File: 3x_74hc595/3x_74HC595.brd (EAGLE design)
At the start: 61 x 19.1 mm, 12 parts, among them IC1 74HC595D, IC2 74HC595D, IC3 74HC595D

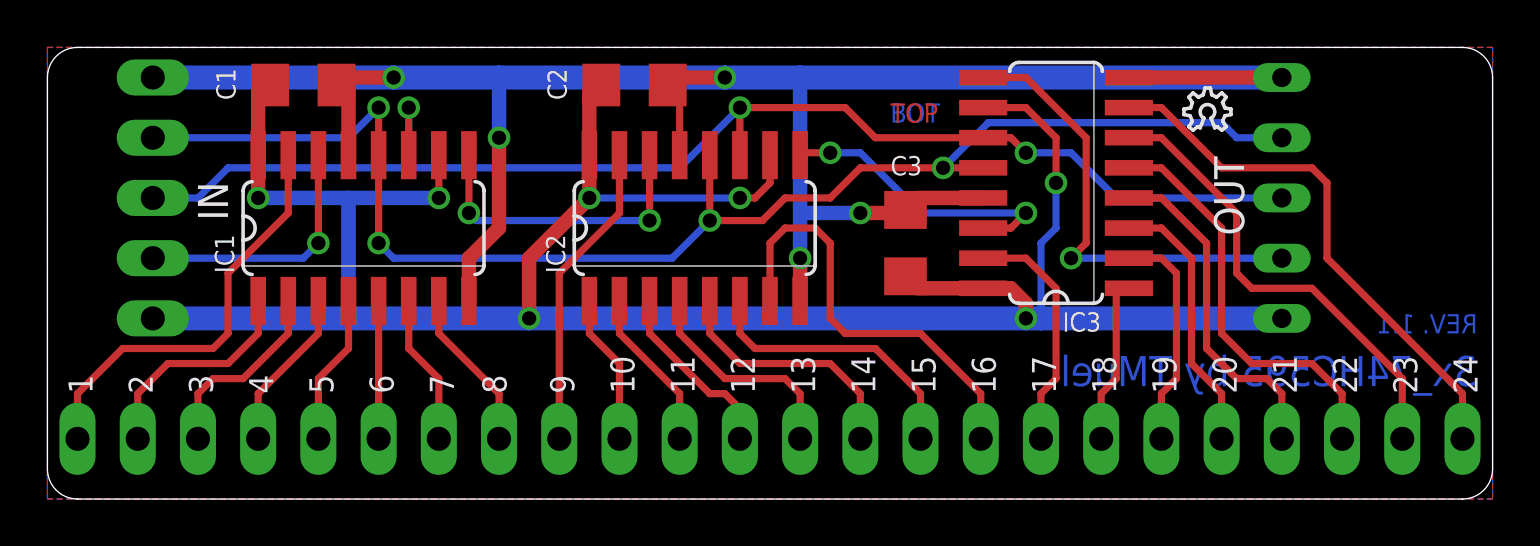
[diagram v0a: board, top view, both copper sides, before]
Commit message: Moved the OUT connector for better daisy chaining
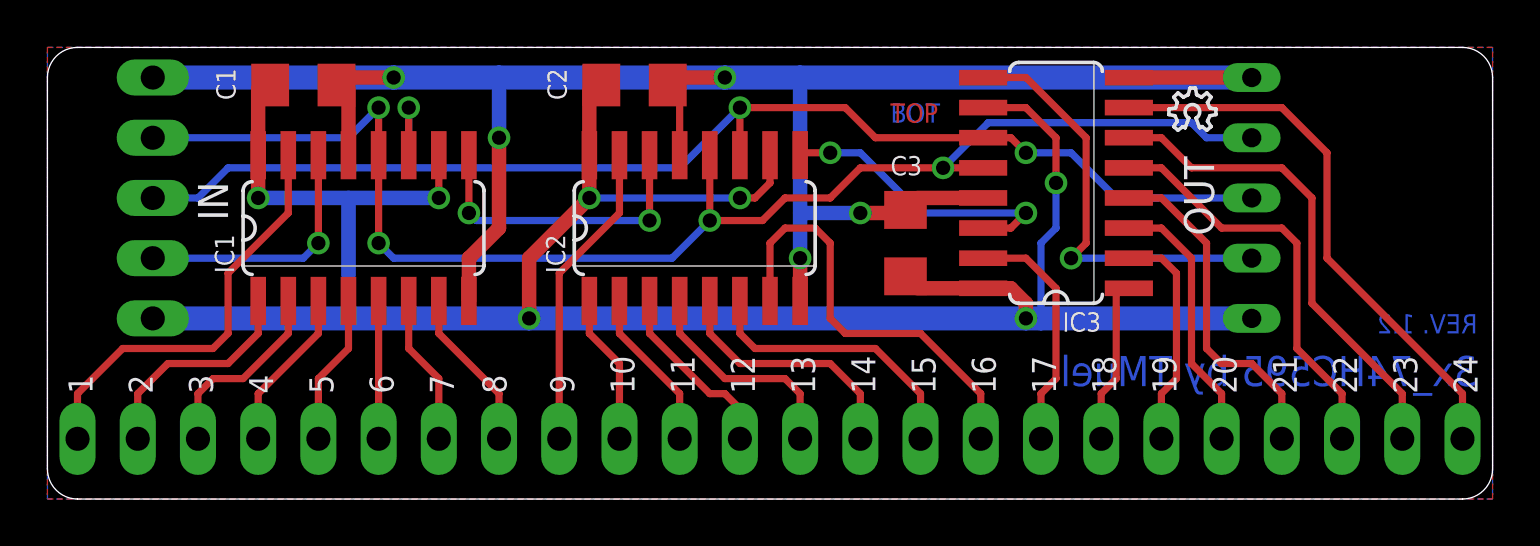
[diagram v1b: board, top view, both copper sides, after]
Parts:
- moved OUT 1.27 mm to (50.8, 12.7)
- moved U$1 0.64 mm to (47.3, 15.6)
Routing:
- net GND: track 93.1 -> 90.5 mm
- net +5V: track 105.3 -> 104.0 mm
- net DATA_OUT: track 19.6 -> 18.4 mm
- net CLK: track 57.3 -> 56.1 mm
- net LATCH: track 61.2 -> 59.9 mm
- net 3QH: track 22.8 -> 23.6 mm
- net 3QG: track 19.8 -> 20.5 mm
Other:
- board text added: "REV 1.1: * Rounded edges for the board outline * Labels for the IO REV 1.2: * Moved the OUT connector for better daisy chaining"
- board text added: "REV. 1.2"
- board text removed: "REV 1.1: * Rounded edges for the board outline * Labels for the IO"
- board text removed: "REV. 1.1"
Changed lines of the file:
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@@
 <setting verticaltext="up"/>
 </settings>
-<grid distance="50" unitdist="mil" unit="mil" style="lines" multiple="1" display="yes" altdistance="0.025" altunitdist="inch" altunit="inch"/>
+<grid distance="25" unitdist="mil" unit="mil" style="lines" multiple="1" display="yes" altdistance="0.025" altunitdist="inch" altunit="inch"/>
 <layers>
 <layer number="1" name="Top" color="4" fill="1" visible="yes" active="yes"/>
@@
 <text x="60.325" y="4.445" size="1.016" layer="21" font="vector" ratio="12" rot="R90">24</text>
 <text x="60.325" y="4.7625" size="1.27" layer="16" font="vector" ratio="12" rot="MR0">3x_74HC595 by TMuel</text>
-<text x="60.325" y="6.985" size="0.8128" layer="16" font="vector" ratio="20" rot="MR0">REV. 1.1</text>
+<text x="60.325" y="6.985" size="0.8128" layer="16" font="vector" ratio="20" rot="MR0">REV. 1.2</text>
 <text x="35.56" y="15.875" size="0.8128" layer="1" font="vector" ratio="20">TOP</text>
 <text x="35.56" y="15.875" size="0.8128" layer="16" font="vector" ratio="20">BOT</text>
 <text x="0" y="20.32" size="1.016" layer="48" font="vector" ratio="12">REV 1.1:
 * Rounded edges for the board outline
-* Labels for the IO</text>
+* Labels for the IO
+REV 1.2:
+* Moved the OUT connector for better daisy chaining</text>
 <text x="60.0075" y="17.4625" size="0.8128" layer="26" font="vector" ratio="12" rot="MR0">GND</text>
 <text x="60.0075" y="7.3025" size="0.8128" layer="26" font="vector" ratio="12" rot="MR0">+5V</text>
@@
 <attribute name="VALUE" x="6.985" y="11.43" size="1.27" layer="28" ratio="10" rot="MR270"/>
 </element>
-<element name="OUT" library="con-lsta" package="FE05W" value="" x="52.07" y="12.7" smashed="yes" rot="MR90">
-<attribute name="OC_NEWARK" value="unknown" x="20.32" y="33.02" size="1.778" layer="28" rot="MR90" display="off"/>
-<attribute name="MPN" value="" x="20.32" y="33.02" size="1.778" layer="28" rot="MR90" display="off"/>
-<attribute name="MF" value="" x="20.32" y="33.02" size="1.778" layer="28" rot="MR90" display="off"/>
-<attribute name="OC_FARNELL" value="unknown" x="20.32" y="33.02" size="1.778" layer="28" rot="MR90" display="off"/>
-<attribute name="NAME" x="50.4825" y="11.1125" size="1.27" layer="25" font="vector" ratio="12" rot="R90"/>
-<attribute name="VALUE" x="54.102" y="8.128" size="1.27" layer="28" ratio="10" rot="MR180"/>
-</element>
-<element name="U$1" library="ohw-logo" package="OSHW_6X70_NOTEXT" value="" x="47.9425" y="15.5575"/>
+<element name="OUT" library="con-lsta" package="FE05W" value="" x="50.8" y="12.7" smashed="yes" rot="MR90">
+<attribute name="OC_NEWARK" value="unknown" x="19.05" y="33.02" size="1.778" layer="28" rot="MR90" display="off"/>
+<attribute name="MPN" value="" x="19.05" y="33.02" size="1.778" layer="28" rot="MR90" display="off"/>
+<attribute name="MF" value="" x="19.05" y="33.02" size="1.778" layer="28" rot="MR90" display="off"/>
+<attribute name="OC_FARNELL" value="unknown" x="19.05" y="33.02" size="1.778" layer="28" rot="MR90" display="off"/>
+<attribute name="NAME" x="49.2125" y="11.1125" size="1.27" layer="25" font="vector" ratio="12" rot="R90"/>
+<attribute name="VALUE" x="52.832" y="8.128" size="1.27" layer="28" ratio="10" rot="MR180"/>
+</element>
+<element name="U$1" library="ohw-logo" package="OSHW_6X70_NOTEXT" value="" x="47.3075" y="15.5575"/>
 </elements>
 <signals>
@@
 <contactref element="SV3" pad="5"/>
 <wire x1="52.07" y1="2.54" x2="52.07" y2="4.445" width="0.3048" layer="1"/>
-<wire x1="52.07" y1="4.445" x2="51.435" y2="5.08" width="0.3048" layer="1"/>
-<wire x1="51.435" y1="5.08" x2="50.165" y2="5.08" width="0.3048" layer="1"/>
-<wire x1="50.165" y1="5.08" x2="48.895" y2="6.35" width="0.3048" layer="1"/>
+<wire x1="52.07" y1="4.445" x2="50.8" y2="5.715" width="0.3048" layer="1"/>
+<wire x1="50.8" y1="5.715" x2="49.53" y2="5.715" width="0.3048" layer="1"/>
+<wire x1="49.53" y1="5.715" x2="48.895" y2="6.35" width="0.3048" layer="1"/>
 <wire x1="48.895" y1="6.35" x2="48.895" y2="10.795" width="0.3048" layer="1"/>
 <wire x1="48.895" y1="10.795" x2="46.99" y2="12.7" width="0.3048" layer="1"/>
@@
 <contactref element="SV3" pad="6"/>
 <wire x1="54.61" y1="2.54" x2="54.61" y2="4.445" width="0.3048" layer="1"/>
-<wire x1="54.61" y1="4.445" x2="53.34" y2="5.715" width="0.3048" layer="1"/>
-<wire x1="53.34" y1="5.715" x2="50.8" y2="5.715" width="0.3048" layer="1"/>
-<wire x1="50.8" y1="5.715" x2="49.53" y2="6.985" width="0.3048" layer="1"/>
-<wire x1="49.53" y1="6.985" x2="49.53" y2="11.43" width="0.3048" layer="1"/>
+<wire x1="54.61" y1="4.445" x2="52.705" y2="6.35" width="0.3048" layer="1"/>
+<wire x1="52.705" y1="6.35" x2="52.705" y2="10.795" width="0.3048" layer="1"/>
+<wire x1="52.705" y1="10.795" x2="52.07" y2="11.43" width="0.3048" layer="1"/>
+<wire x1="52.07" y1="11.43" x2="49.53" y2="11.43" width="0.3048" layer="1"/>
 <wire x1="49.53" y1="11.43" x2="46.99" y2="13.97" width="0.3048" layer="1"/>
 <wire x1="46.99" y1="13.97" x2="45.6184" y2="13.97" width="0.3048" layer="1"/>
@@
 <contactref element="IC3" pad="6"/>
 <contactref element="SV3" pad="7"/>
-<wire x1="57.15" y1="2.54" x2="57.15" y2="5.08" width="0.3048" layer="1"/>
-<wire x1="57.15" y1="5.08" x2="53.34" y2="8.89" width="0.3048" layer="1"/>
-<wire x1="53.34" y1="8.89" x2="50.8" y2="8.89" width="0.3048" layer="1"/>
-<wire x1="50.8" y1="8.89" x2="50.165" y2="9.525" width="0.3048" layer="1"/>
-<wire x1="50.165" y1="9.525" x2="50.165" y2="12.065" width="0.3048" layer="1"/>
-<wire x1="50.165" y1="12.065" x2="46.99" y2="15.24" width="0.3048" layer="1"/>
+<wire x1="57.15" y1="2.54" x2="57.15" y2="4.445" width="0.3048" layer="1"/>
+<wire x1="57.15" y1="4.445" x2="53.34" y2="8.255" width="0.3048" layer="1"/>
+<wire x1="53.34" y1="8.255" x2="53.34" y2="12.7" width="0.3048" layer="1"/>
+<wire x1="53.34" y1="12.7" x2="52.07" y2="13.97" width="0.3048" layer="1"/>
+<wire x1="52.07" y1="13.97" x2="48.26" y2="13.97" width="0.3048" layer="1"/>
+<wire x1="48.26" y1="13.97" x2="46.99" y2="15.24" width="0.3048" layer="1"/>
 <wire x1="46.99" y1="15.24" x2="45.6184" y2="15.24" width="0.3048" layer="1"/>
 </signal>
@@
 <wire x1="59.69" y1="2.54" x2="59.69" y2="4.445" width="0.3048" layer="1"/>
 <wire x1="59.69" y1="4.445" x2="53.975" y2="10.16" width="0.3048" layer="1"/>
-<wire x1="53.975" y1="10.16" x2="53.975" y2="13.335" width="0.3048" layer="1"/>
-<wire x1="53.975" y1="13.335" x2="53.34" y2="13.97" width="0.3048" layer="1"/>
-<wire x1="53.34" y1="13.97" x2="49.53" y2="13.97" width="0.3048" layer="1"/>
-<wire x1="49.53" y1="13.97" x2="46.99" y2="16.51" width="0.3048" layer="1"/>
-<wire x1="46.99" y1="16.51" x2="45.6184" y2="16.51" width="0.3048" layer="1"/>
+<wire x1="53.975" y1="10.16" x2="53.975" y2="14.605" width="0.3048" layer="1"/>
+<wire x1="53.975" y1="14.605" x2="52.07" y2="16.51" width="0.3048" layer="1"/>
+<wire x1="52.07" y1="16.51" x2="45.6184" y2="16.51" width="0.3048" layer="1"/>
 </signal>
 <signal name="+5V">
@@
 <wire x1="22.86" y1="14.5034" x2="22.86" y2="17.275" width="0.6096" layer="1"/>
 <wire x1="22.86" y1="17.275" x2="23.365" y2="17.4625" width="0.3048" layer="1"/>
-<wire x1="52.07" y1="7.62" x2="41.91" y2="7.62" width="1.016" layer="16"/>
+<wire x1="50.8" y1="7.62" x2="41.91" y2="7.62" width="1.016" layer="16"/>
 <wire x1="41.91" y1="7.62" x2="41.275" y2="7.62" width="1.016" layer="16"/>
 <wire x1="41.275" y1="7.62" x2="20.32" y2="7.62" width="1.016" layer="16"/>
@@
 <wire x1="26.67" y1="14.5034" x2="26.67" y2="17.275" width="0.3048" layer="1"/>
 <wire x1="26.67" y1="17.275" x2="26.165" y2="17.4625" width="0.3048" layer="1"/>
-<wire x1="52.07" y1="17.78" x2="31.75" y2="17.78" width="1.016" layer="16"/>
+<wire x1="50.8" y1="17.78" x2="31.75" y2="17.78" width="1.016" layer="16"/>
 <wire x1="31.75" y1="17.78" x2="28.575" y2="17.78" width="1.016" layer="16"/>
 <wire x1="28.575" y1="17.78" x2="19.05" y2="17.78" width="1.016" layer="16"/>
 <wire x1="19.05" y1="17.78" x2="14.605" y2="17.78" width="1.016" layer="16"/>
 <wire x1="14.605" y1="17.78" x2="4.445" y2="17.78" width="1.016" layer="16"/>
-<wire x1="45.6184" y1="17.78" x2="52.07" y2="17.78" width="0.6096" layer="1"/>
+<wire x1="45.6184" y1="17.78" x2="50.8" y2="17.78" width="0.6096" layer="1"/>
 <wire x1="31.75" y1="8.3566" x2="31.75" y2="10.16" width="0.6096" layer="1"/>
 <via x="31.75" y="10.16" extent="1-16" drill="0.6" shape="octagon"/>
@@
 <wire x1="7.62" y1="13.97" x2="15.24" y2="13.97" width="0.3048" layer="16"/>
 <wire x1="15.24" y1="13.97" x2="15.24" y2="16.51" width="0.3048" layer="16"/>
-<wire x1="52.07" y1="12.7" x2="45.085" y2="12.7" width="0.3048" layer="16"/>
+<wire x1="50.8" y1="12.7" x2="45.085" y2="12.7" width="0.3048" layer="16"/>
 <via x="41.275" y="14.605" extent="1-16" drill="0.6" shape="octagon"/>
 <wire x1="41.275" y1="14.605" x2="43.18" y2="14.605" width="0.3048" layer="16"/>
@@
 <via x="13.97" y="10.795" extent="1-16" drill="0.6" shape="octagon"/>
 <wire x1="13.97" y1="10.795" x2="13.97" y2="14.5034" width="0.3048" layer="1"/>
-<wire x1="52.07" y1="15.24" x2="50.165" y2="15.24" width="0.3048" layer="16"/>
-<wire x1="50.165" y1="15.24" x2="49.53" y2="15.875" width="0.3048" layer="16"/>
-<wire x1="49.53" y1="15.875" x2="39.6875" y2="15.875" width="0.3048" layer="16"/>
+<wire x1="50.8" y1="15.24" x2="48.895" y2="15.24" width="0.3048" layer="16"/>
+<wire x1="48.895" y1="15.24" x2="48.26" y2="15.875" width="0.3048" layer="16"/>
+<wire x1="48.26" y1="15.875" x2="39.6875" y2="15.875" width="0.3048" layer="16"/>
 <wire x1="39.6875" y1="15.875" x2="37.7825" y2="13.97" width="0.3048" layer="16"/>
 <wire x1="37.7825" y1="13.97" x2="39.4716" y2="13.97" width="0.3048" layer="1"/>
@@
 <wire x1="43.815" y1="10.795" x2="43.18" y2="10.16" width="0.3048" layer="1"/>
 <via x="43.18" y="10.16" extent="1-16" drill="0.6" shape="octagon"/>
-<wire x1="43.18" y1="10.16" x2="52.07" y2="10.16" width="0.3048" layer="16"/>
+<wire x1="43.18" y1="10.16" x2="50.8" y2="10.16" width="0.3048" layer="16"/>
 </signal>
 </signals>
